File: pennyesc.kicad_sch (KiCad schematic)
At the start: 22 parts, among them U1 MA782GGU-Z, U2 STM32L011F4Ux, U3 MP6536DU-LF-Z, U4 LM1117LD-3.3, U5 LM3480-3.3

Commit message: pin assignment with stm32cube, pick LDO
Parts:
- removed U4: LM1117LD-3.3, Package_SON:WSON-8-1EP_4x4mm_P0.8mm_EP2.2x3mm, symbol Regulator_Linear:LM1117LD-3.3
- removed U5: LM3480-3.3, Package_TO_SOT_SMD:SOT-23, symbol Regulator_Linear:LM3480-3.3
- added J2: Conn_01x04, symbol Connector_Generic:Conn_01x04
- added U6: XC6206P332MR-G, Package_TO_SOT_SMD:SOT-23-3, symbol Regulator_Linear:XC6206PxxxMR
- TP3: value U -> P1
- TP4: value U -> P2
- TP5: value U -> P3
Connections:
- net +3.3V: now also U1.11 (EN), U3.15 (SHDNB), U6.3 (VI)
- net GND: now also U1.6 (ASC), J2.1 (Pin_1), U6.1 (GND)
- net PWM1: now reaches U3.12 (PWM1)
- net PWM2: now reaches U3.13 (PWM2)
- net PWM3: now reaches U3.16 (PWM3)
- net STBY: now reaches U3.17 (STBYB)
- net VBUS: now reaches C1.1, TP1.1, U3.26 (VSP), U3.27 (VSP), U3.28 (VSP), U3.3 (VSP), U3.4 (VSP), U3.5 (VSP)
- net VBUS: now also J2.4 (Pin_4), U6.2 (VO)
- net SPI_MOSI: now reaches U2.10 (PA7)
- net SPI_MOSI: now also U1.8 (MOSI)
- net UART_TX: now reaches U2.14 (PA9)
- net UART_RX: now reaches U2.15 (PA10)
- net UART_DE: now reaches U2.6 (PA1)
- net SPI_SCLK: now reaches U2.8 (PA5)
- net SPI_SCLK: now also U1.1 (SCLK)
- net SPI_MISO: now reaches U2.9 (PA6)
- net SPI_MISO: now also U1.5 (MISO)
- net SPI_CS: now reaches U1.7 (/CS)
- no-connect marks 0 -> 4
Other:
- note added: "BOOT0"
- note added: "always active"
- note added: "low for high-z phases internal pulldown"
- note removed: "BOOT0 (check!)"
- moved on the sheet: C1, TP1

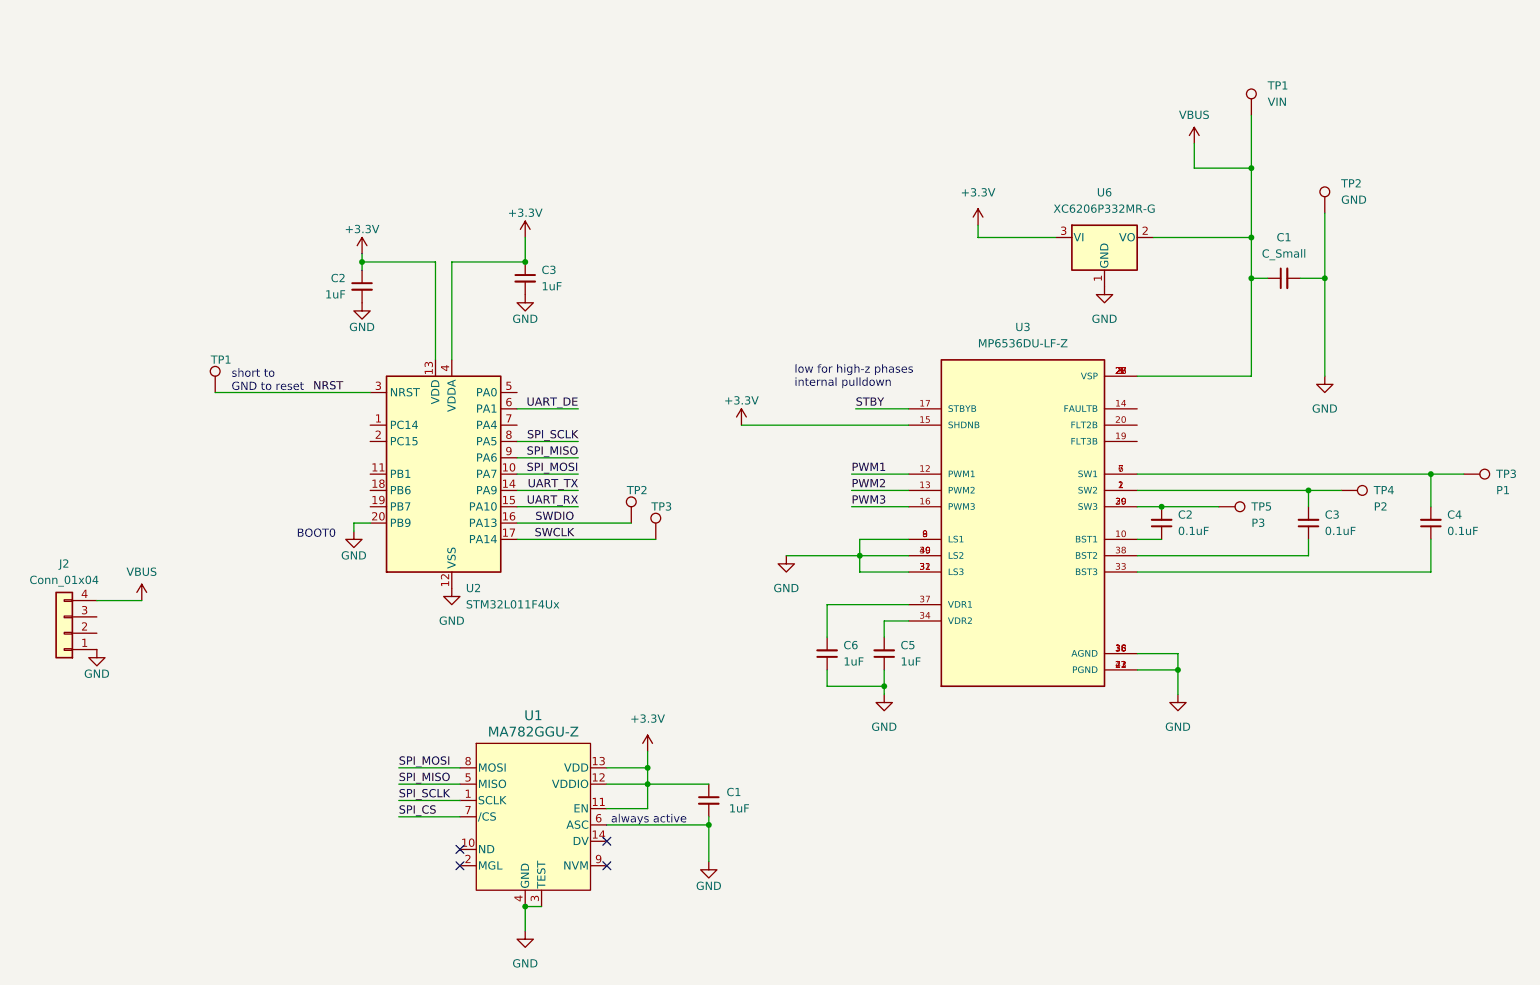
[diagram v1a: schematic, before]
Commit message: switch to cheaper TI parts, passthrough shaft
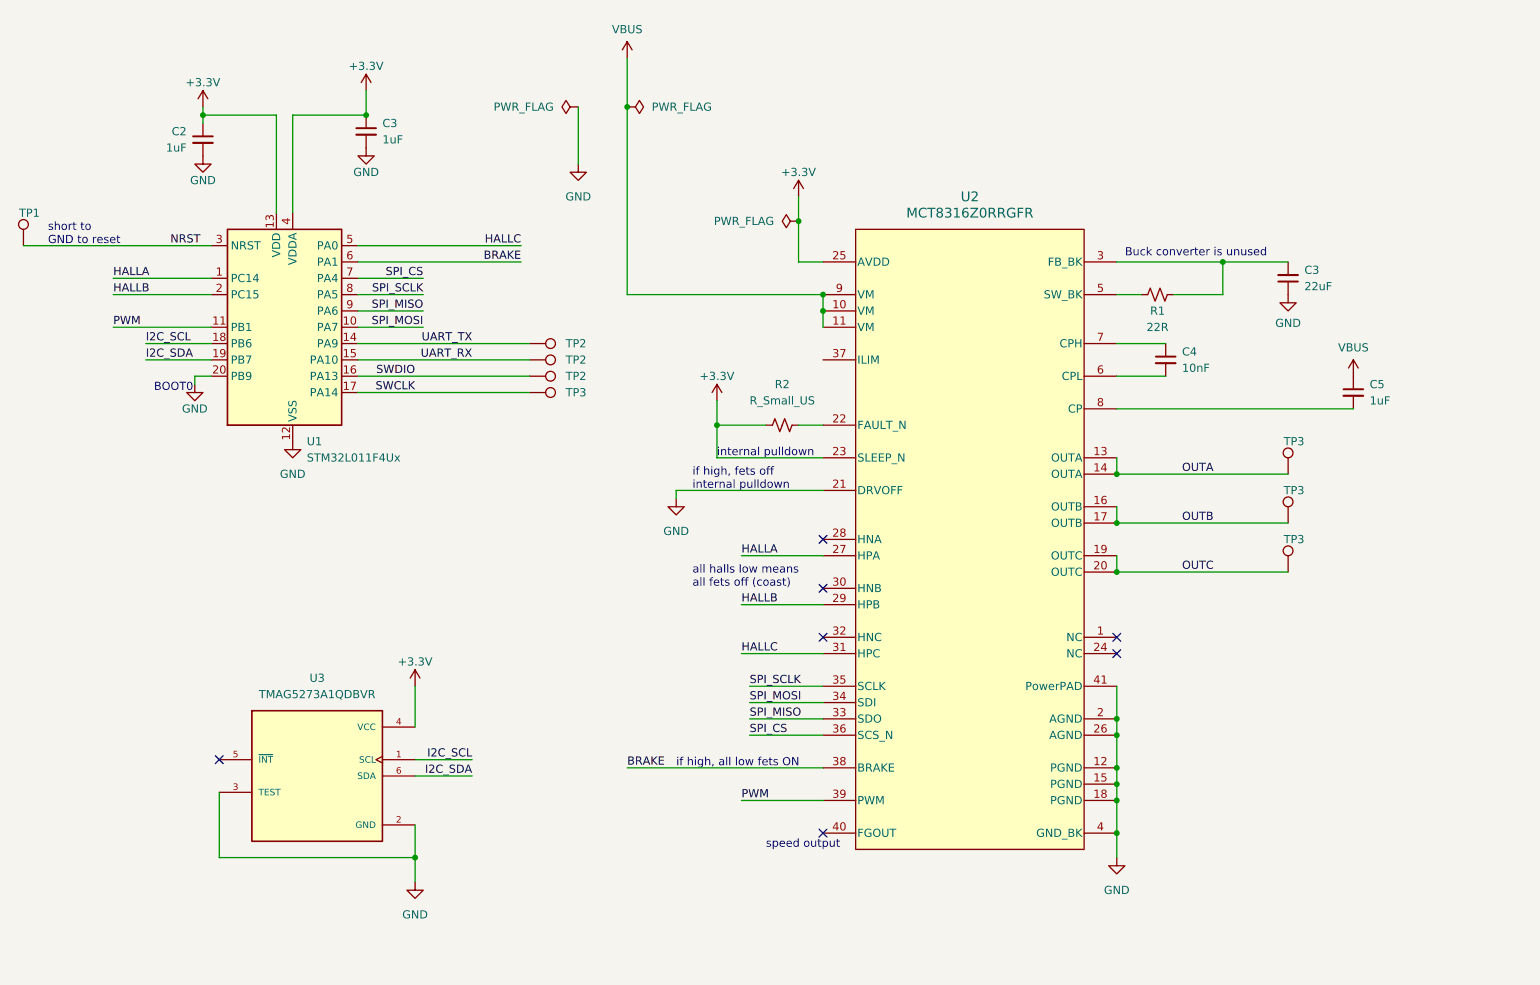
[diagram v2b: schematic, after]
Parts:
- removed C1, C6: 1uF, Capacitor_SMD:C_0402_1005Metric, symbol Device:C_Small
- removed C1: C_Small, Capacitor_SMD:C_0402_1005Metric, symbol Device:C_Small
- removed C2: 0.1uF, Capacitor_SMD:C_0402_1005Metric, symbol Device:C_Small
- removed J2: Conn_01x04, symbol Connector_Generic:Conn_01x04
- removed TP1: VIN, symbol Connector:TestPoint
- removed TP2: GND, symbol Connector:TestPoint
- removed TP3: P1, symbol Connector:TestPoint
- removed TP4: P2, symbol Connector:TestPoint
- removed TP5: P3, symbol Connector:TestPoint
- removed U1: MA782GGU-Z, QFN-14_MA782_MNP, symbol pennyesc:MA782GGU-Z
- removed U3: MP6536DU-LF-Z, pennyesc:QFN40P500X500X100-41N_MP6536DU-LF-Z, symbol pennyesc:MP6536DU-LF-Z
- removed U6: XC6206P332MR-G, Package_TO_SOT_SMD:SOT-23-3, symbol Regulator_Linear:XC6206PxxxMR
- added R1: 22R, Resistor_SMD:R_0402_1005Metric, symbol Device:R_Small_US
- added R2: R_Small_US, symbol Device:R_Small_US
- added TP2 (x2), TP3 (x3): TestPoint, pennyesc:TestPoint_Pad_Rect, symbol Connector:TestPoint
- added U2: MCT8316Z0RRGFR, pennyesc:MCT8316Z0RRGFR-IPC_C, symbol pennyesc:MCT8316Z0RRGFR
- added U3: TMAG5273A1QDBVR, pennyesc:SOT95P280X140-6N, symbol pennyesc:TMAG5273A1QDBVR
- C3: value 0.1uF -> 22uF; footprint Capacitor_SMD:C_0402_1005Metric -> Capacitor_SMD:C_0603_1608Metric; JLCPCB (none) -> C59461; MP (none) -> CL10A226MQ8NRNC
- C4: value 0.1uF -> 10nF; footprint Capacitor_SMD:C_0402_1005Metric -> (none)
- C5: footprint Capacitor_SMD:C_0402_1005Metric -> (none)
- TP1: footprint O12encoder:TestPoint_Pad_Rect -> pennyesc:TestPoint_Pad_Rect
- TP2, TP3: footprint (none) -> pennyesc:TestPoint_Pad_Rect
- renumbered U2 to U1
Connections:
- net +3.3V: now also R2.1, U2.23 (SLEEP_N), U2.25 (AVDD), U3.4 (VCC)
- net GND: now also C3.1, U2.12 (PGND), U2.15 (PGND), U2.18 (PGND), U2.2 (AGND), U2.21 (DRVOFF), U2.26 (AGND), U2.4 (GND_BK), U2.41 (PowerPAD), U3.2 (GND), U3.3 (TEST); no longer C5.1
- net SPI_CS: now also U1.7 (PA4), U2.36 (SCS_N)
- net SPI_MISO: now also U2.33 (SDO)
- net SPI_MOSI: now also U2.34 (SDI)
- net SPI_SCLK: now also U2.35 (SCLK)
- net UART_RX: now also TP2.1
- net UART_TX: now also TP2.1
- net VBUS: now also C5.1, U2.10 (VM), U2.11 (VM), U2.9 (VM)
- net at C3.2: now also R1.2, U2.3 (FB_BK)
- net at C4.1: now also U2.7 (CPH)
- net at C5.2: now also U2.8 (CP)
- net at C4.2: now also U2.6 (CPL)
- net HALLA: now reaches U1.1 (PC14)
- net HALLA: now also U2.27 (HPA)
- net PWM: now reaches U1.11 (PB1)
- net PWM: now also U2.39 (PWM)
- net I2C_SCL: now reaches U1.18 (PB6)
- net I2C_SCL: now also U3.1 (SCL)
- net I2C_SDA: now reaches U1.19 (PB7)
- net I2C_SDA: now also U3.6 (SDA)
- net HALLB: now reaches U1.2 (PC15)
- net HALLB: now also U2.29 (HPB)
- net HALLC: now reaches U1.5 (PA0)
- net HALLC: now also U2.31 (HPC)
- net UART_DE renamed BRAKE
- net BRAKE: now also U2.38 (BRAKE)
- new net: R1.1, U2.5 (SW_BK)
- new net: R2.2, U2.22 (FAULT_N)
- new net OUTA: TP3.1, U2.13 (OUTA), U2.14 (OUTA)
- new net OUTB: TP3.1, U2.16 (OUTB), U2.17 (OUTB)
- new net OUTC: TP3.1, U2.19 (OUTC), U2.20 (OUTC)
- no-connect marks 4 -> 7
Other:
- note added: "Buck converter is unused"
- note added: "all halls low means all fets off (coast)"
- note added: "if high, all low fets ON"
- note added: "if high, fets off internal pulldown"
- note added: "internal pulldown"
- note added: "speed output"
- note removed: "always active"
- note removed: "low for high-z phases internal pulldown"
- moved on the sheet: C2, C3, TP1, TP2, TP3, U1

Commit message: chose R and C values, set jlcpcb constraints, started layout
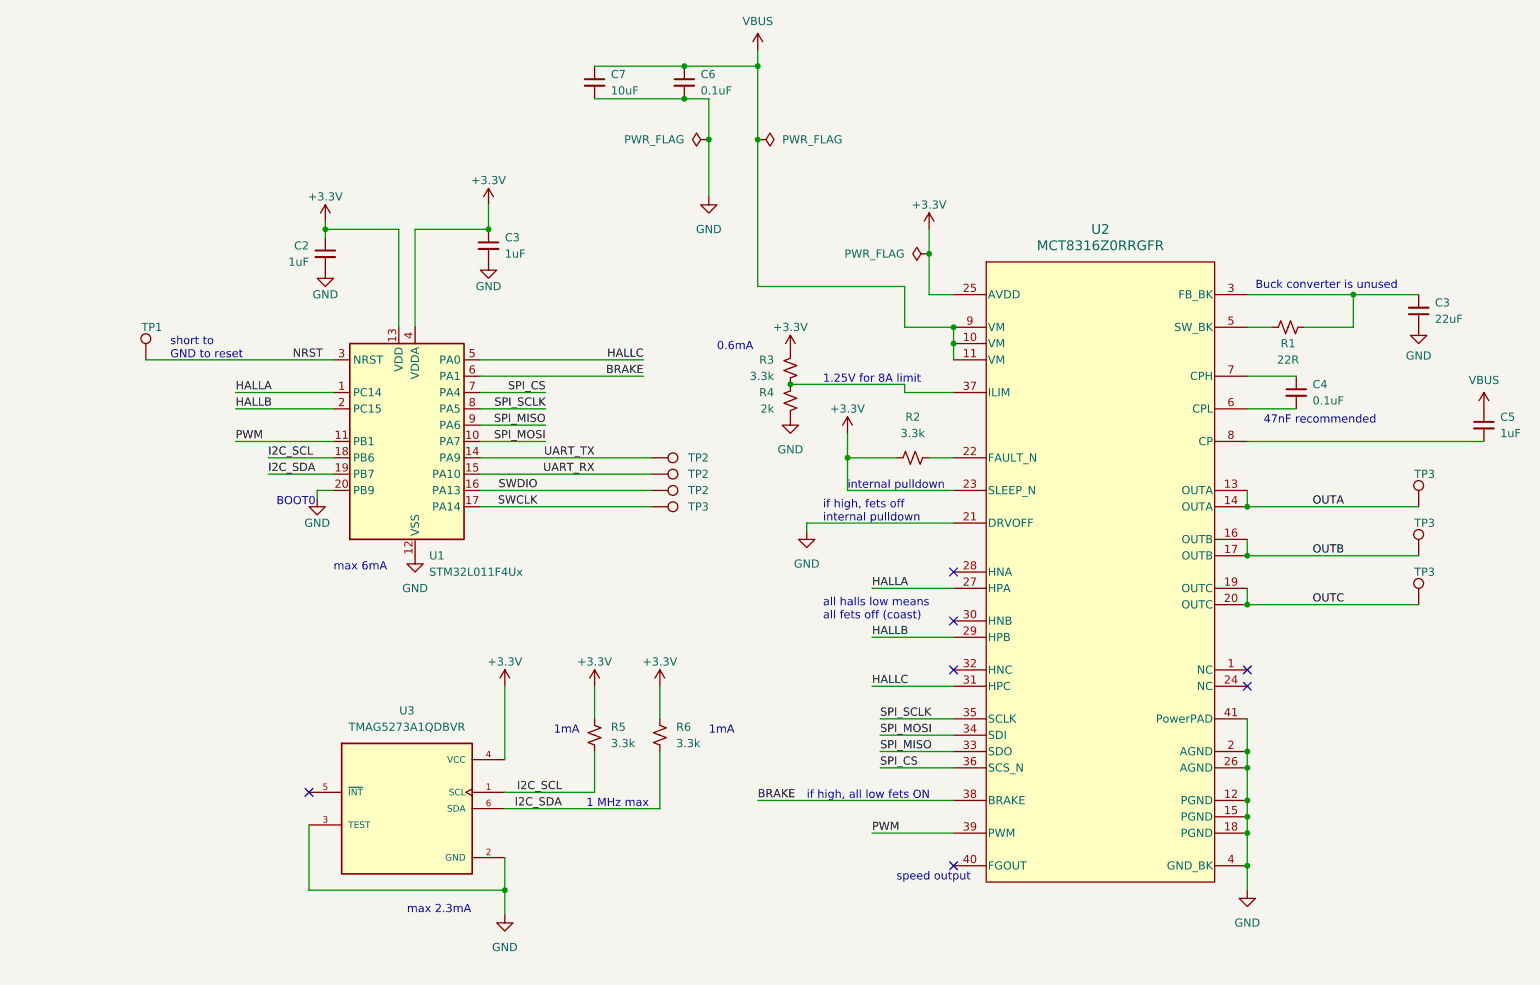
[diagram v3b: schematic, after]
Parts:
- added C6: 0.1uF, Capacitor_SMD:C_0402_1005Metric, symbol Device:C_Small
- added C7: 10uF, Capacitor_SMD:C_0603_1608Metric, symbol Device:C_Small
- added R3, R5, R6: 3.3k, Resistor_SMD:R_0402_1005Metric, symbol Device:R_Small_US
- added R4: 2k, Resistor_SMD:R_0402_1005Metric, symbol Device:R_Small_US
- C2, C3: JLCPCB (none) -> C52923; MP (none) -> CL05A105KA5NQNC
- C4: value 10nF -> 0.1uF; footprint (none) -> Capacitor_SMD:C_0402_1005Metric; JLCPCB (none) -> C307331; MP (none) -> CL05B104KB54PNC
- C5: footprint (none) -> Capacitor_SMD:C_0402_1005Metric; JLCPCB (none) -> C52923; MP (none) -> CL05A105KA5NQNC
- R2: value R_Small_US -> 3.3k; footprint (none) -> Resistor_SMD:R_0402_1005Metric; JLCPCB (none) -> C25890; MP (none) -> 0402WGF3301TCE
- TP3: footprint pennyesc:TestPoint_Pad_Rect -> pennyesc:SolderHole_1.0x1.6mm
- U1: JLCPCB (none) -> C329283; MP (none) -> STM32L011F4U6TR
- U2: JLCPCB (none) -> C3681249; MP (none) -> MCT8316Z0RRGFR
- U3: JLCPCB (none) -> C3716049
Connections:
- net +3.3V: now also R3.1, R5.1, R6.1
- net GND: now also C6.2, C7.2, R4.2
- net I2C_SCL: now also R5.2
- net I2C_SDA: now also R6.2
- net VBUS: now also C6.1, C7.1
- net at U2.37 (ILIM): now also R3.2, R4.1
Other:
- note added: "0.6mA"
- note added: "1 MHz max"
- note added: "1.25V for 8A limit"
- note added: "1mA"
- note added: "47nF recommended"
- note added: "max 2.3mA"
- note added: "max 6mA"
- moved on the sheet: C2, C3, C4, C5, R1, R2, TP1, TP2, TP3, U1, U2, U3

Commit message: finish v1 and order from jlcpcb
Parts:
- added TP1: TestPoint, pennyesc:TestPoint_Pad_1mm, symbol Connector:TestPoint
- added TP2 (x2): TestPoint, pennyesc:Power_Pad_Rect, symbol Connector:TestPoint
- C2, C3, C5: LCSC PN (none) -> C52923
- C3: LCSC PN (none) -> C59461
- C4, C6: LCSC PN (none) -> C307331
- C7: LCSC PN (none) -> C96446
- R1: LCSC PN (none) -> C25092
- R2, R3, R5, R6: LCSC PN (none) -> C25890
- R4: LCSC PN (none) -> C4109
- TP1: footprint pennyesc:TestPoint_Pad_Rect -> pennyesc:TestPoint_Pad_1mm
- U1: FT Rotation Offset (none) -> 180; LCSC PN (none) -> C329283
- U2: LCSC PN (none) -> C3681249
- U3: FT Rotation Offset (none) -> 180; LCSC PN (none) -> C3716049
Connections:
- net GND: now also TP1.1, TP2.1
- net VBUS: now also TP2.1

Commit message: octant LUT for off axis magnetic encoder, staircase artifacts left
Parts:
- added R8: 3.3k, Resistor_SMD:R_0402_1005Metric, symbol Device:R_Small_US
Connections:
- net +3.3V: now also R8.1
- net UART_RX: now also R8.2
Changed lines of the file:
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@@
   (junction (at 140.97 76.2) (diameter 0) (color 0 0 0 0)
+  )
+  (junction (at 118.11 90.17) (diameter 0) (color 0 0 0 0)
   )
   (junction (at 212.09 102.87) (diameter 0) (color 0 0 0 0)
@@
     (stroke (width 0) (type default))
   )
-  (wire (pts (xy 92.71 90.17) (xy 119.38 90.17))
+  (wire (pts (xy 92.71 90.17) (xy 118.11 90.17))
     (stroke (width 0) (type default))
   )
@@
     (stroke (width 0) (type default))
   )
+  (wire (pts (xy 124.46 82.55) (xy 118.11 82.55))
+    (stroke (width 0) (type default))
+  )
   (wire (pts (xy 68.58 50.8) (xy 68.58 52.07))
     (stroke (width 0) (type default))
@@
     (stroke (width 0) (type default))
   )
+  (wire (pts (xy 118.11 90.17) (xy 119.38 90.17))
+    (stroke (width 0) (type default))
+  )
   (wire (pts (xy 154.94 128.27) (xy 166.37 128.27))
     (stroke (width 0) (type default))
@@
   )
   (wire (pts (xy 228.6 67.31) (xy 228.6 62.23))
+    (stroke (width 0) (type default))
+  )
+  (wire (pts (xy 118.11 82.55) (xy 118.11 90.17))
     (stroke (width 0) (type default))
   )
@@
         (path "/ccc85adb-68fc-4d61-8791-18046cba3493"
           (reference "R5") (unit 1)
+        )
+      )
+    )
+  )
+  (symbol (lib_id "power:+3.3V") (at 124.46 77.47 0) (mirror y) (unit 1)
+    (in_bom yes) (on_board yes) (dnp no)
+    (property "Reference" "#PWR013" (at 124.46 81.28 0)
+      (effects (font (size 1.27 1.27)) hide)
+    )
+    (property "Value" "+3.3V" (at 124.46 73.66 0)
+      (effects (font (size 1.27 1.27)))
+    )
+    (property "Footprint" "" (at 124.46 77.47 0)
+      (effects (font (size 1.27 1.27)) hide)
+    )
+    (property "Datasheet" "" (at 124.46 77.47 0)
+      (effects (font (size 1.27 1.27)) hide)
+    )
+    (pin "1")
+    (instances
+      (project "O12encoder"
+        (path "/272cfae1-2e7a-4cac-b2e0-2058a01f6a29"
+          (reference "#PWR013") (unit 1)
+        )
+      )
+      (project "O32controller"
+        (path "/af2b7c4e-7b6b-40c8-b9a1-0c412d67fa31"
+          (reference "#PWR032") (unit 1)
+        )
+      )
+      (project "pennyesc"
+        (path "/ccc85adb-68fc-4d61-8791-18046cba3493"
+          (reference "#PWR022") (unit 1)
         )
       )
@@
         )
       )
+    )
+  )
+  (symbol (lib_id "Device:R_Small_US") (at 124.46 80.01 0) (mirror y) (unit 1)
+    (in_bom yes) (on_board yes) (dnp no)
+    (property "Reference" "R8" (at 121.92 78.74 0)
+      (effects (font (size 1.27 1.27)) (justify left))
+    )
+    (property "Value" "3.3k" (at 121.92 81.28 0)
+      (effects (font (size 1.27 1.27)) (justify left))
+    )
+    (property "Footprint" "Resistor_SMD:R_0402_1005Metric" (at 124.46 80.01 0)
+      (effects (font (size 1.27 1.27)) hide)
+    )
+    (property "Datasheet" "~" (at 124.46 80.01 0)
+      (effects (font (size 1.27 1.27)) hide)
+    )
+    (property "JLCPCB" "C25890" (at 124.46 80.01 0)
+      (effects (font (size 1.27 1.27)) hide)
+    )
+    (property "MP" "0402WGF3301TCE" (at 124.46 80.01 0)
+      (effects (font (size 1.27 1.27)) hide)
+    )
+    (property "LCSC PN" "C25890" (at 124.46 80.01 0)
+      (effects (font (size 1.27 1.27)) hide)
+    )
+    (property "FT Rotation Offset" "" (at 124.46 80.01 0)
+      (effects (font (size 1.27 1.27)) hide)
+    )
+    (pin "1")
+    (pin "2")
+    (instances
+      (project "pennyesc"
+        (path "/ccc85adb-68fc-4d61-8791-18046cba3493"
+          (reference "R8") (unit 1)
+        )
+      )

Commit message: encoder and magpoll gui
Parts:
- renumbered C3 to C1, TP2 to TP10, TP1 to TP11, TP2 to TP3, TP2 to TP4, TP3 to TP5, TP3 to TP6, TP3 to TP7, TP3 to TP8, TP2 to TP9

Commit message: faultn pullup should be 1k
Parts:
- R2: value 3.3k -> 1k
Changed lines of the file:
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@@
 			)
 		)
-		(property "Value" "3.3k"
+		(property "Value" "1k"
 			(at 160.02 83.82 90)
 			(show_name no)
